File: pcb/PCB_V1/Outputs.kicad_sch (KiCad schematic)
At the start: 18 parts, among them J501 FAN1 / WAGO 2601, J511 FAN2 / WAGO 2601, J521 PUMP + / switched -, Q501 AO3400A, Q511 AO3400A, Q521 AO3400A

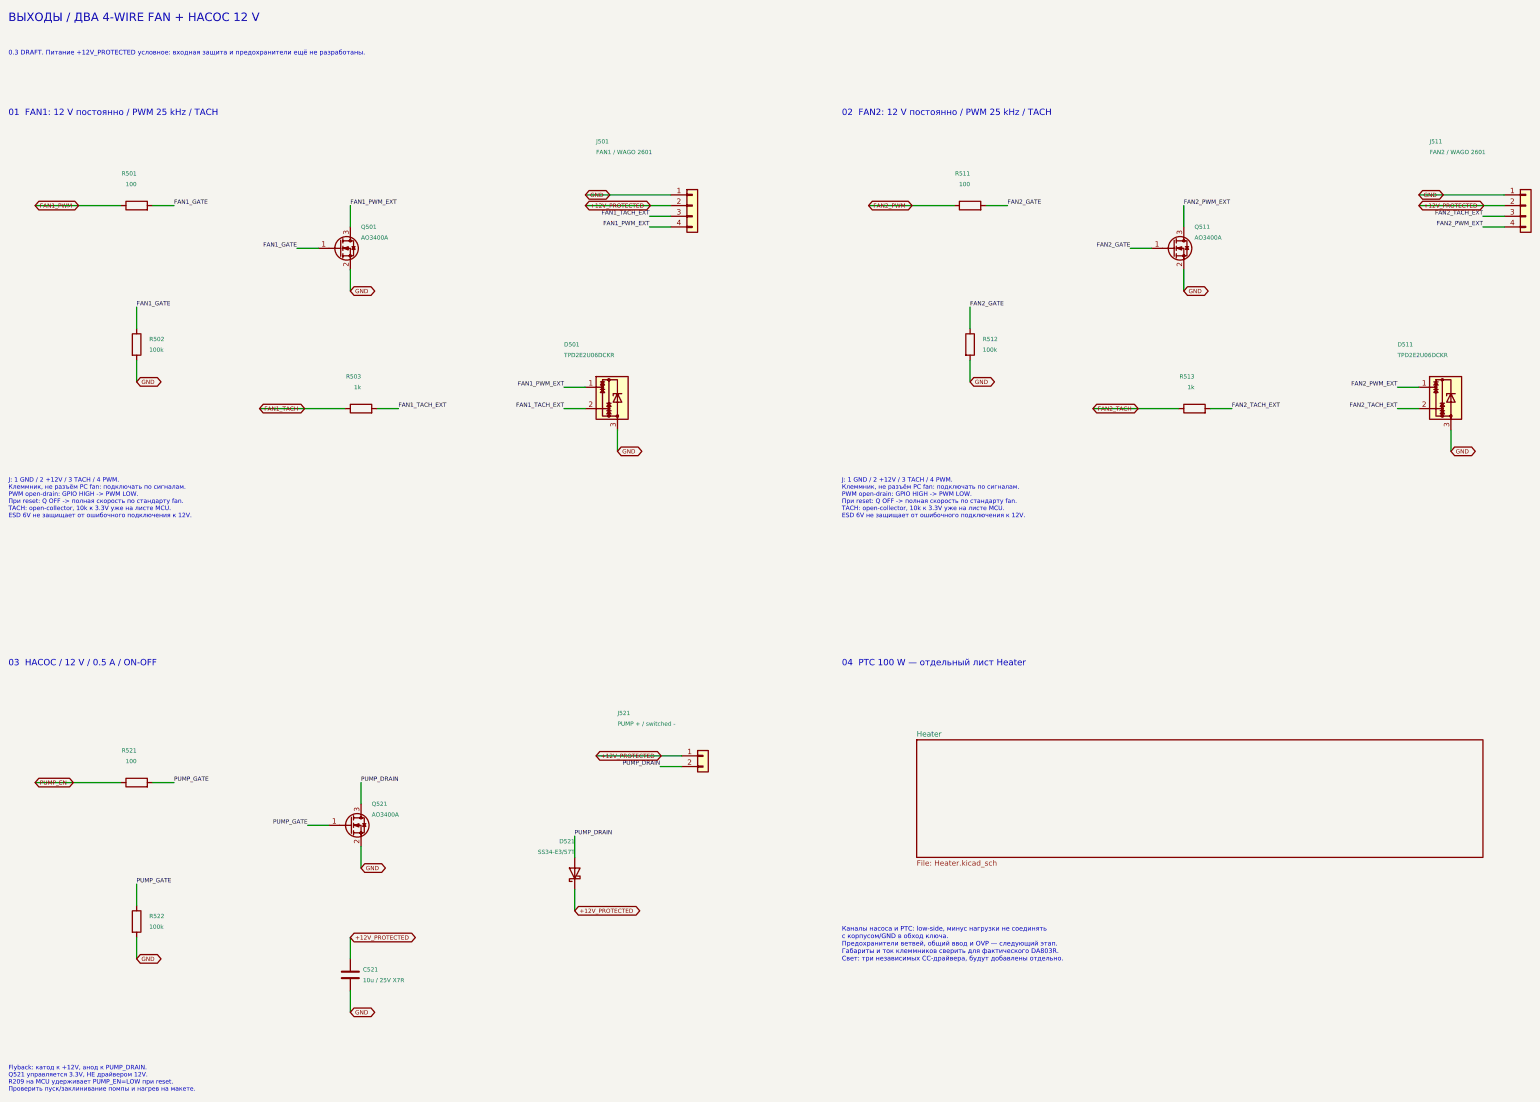
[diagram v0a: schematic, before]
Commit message: pcb: add protected input and independent LED boost drivers
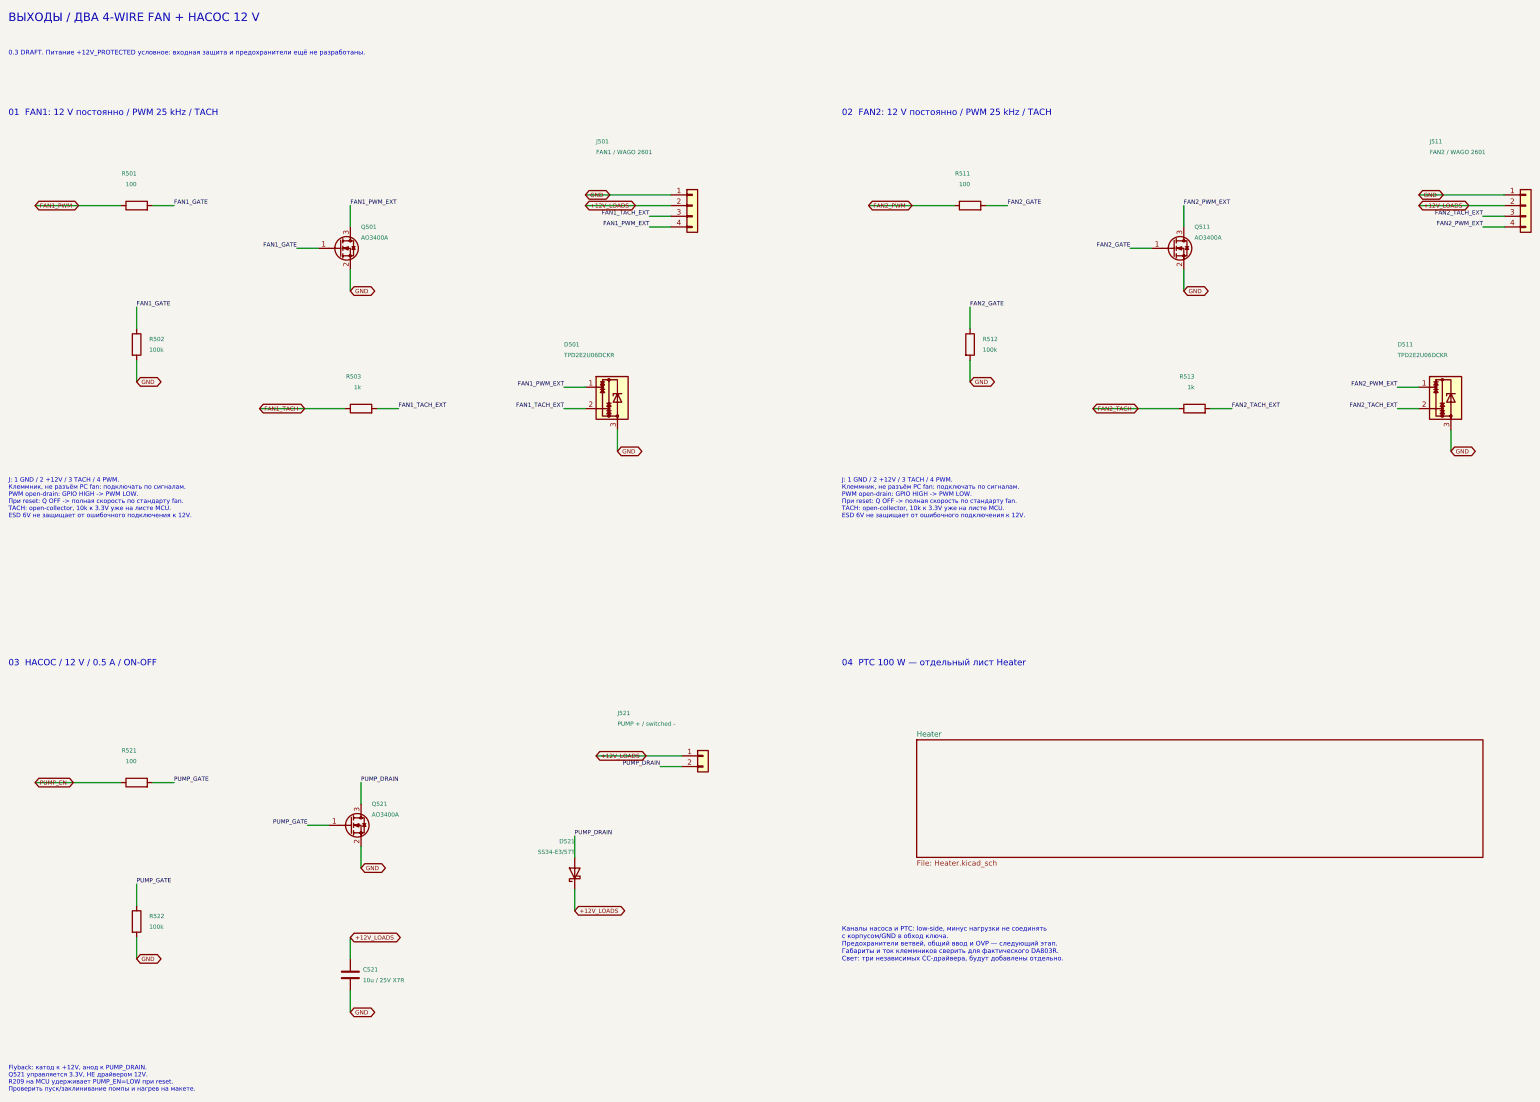
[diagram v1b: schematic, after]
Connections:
- net +12V_PROTECTED renamed +12V_LOADS
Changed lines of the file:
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@@
 		(title "04 - Fans and pump")
 		(date "2026-09-26")
-		(rev "0.3-DRAFT")
+		(rev "0.4-DRAFT")
 		(company "GrowBox controller")
 		(comment 1 "Draft: input protection and LED drivers pending")
@@
 		)
 	)
-	(global_label "+12V_PROTECTED"
+	(global_label "+12V_LOADS"
 		(shape bidirectional)
 		(at 355.6 60.96 0)
@@
 		)
 	)
-	(global_label "+12V_PROTECTED"
+	(global_label "+12V_LOADS"
 		(shape bidirectional)
 		(at 154.94 228.6 0)
@@
 		)
 	)
-	(global_label "+12V_PROTECTED"
+	(global_label "+12V_LOADS"
 		(shape bidirectional)
 		(at 157.48 60.96 0)
@@
 		)
 	)
-	(global_label "+12V_PROTECTED"
+	(global_label "+12V_LOADS"
 		(shape bidirectional)
 		(at 160.02 191.77 0)
@@
 		)
 	)
-	(global_label "+12V_PROTECTED"
+	(global_label "+12V_LOADS"
 		(shape bidirectional)
 		(at 101.6 234.95 0)
